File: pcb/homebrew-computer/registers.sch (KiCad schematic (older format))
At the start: 24 parts

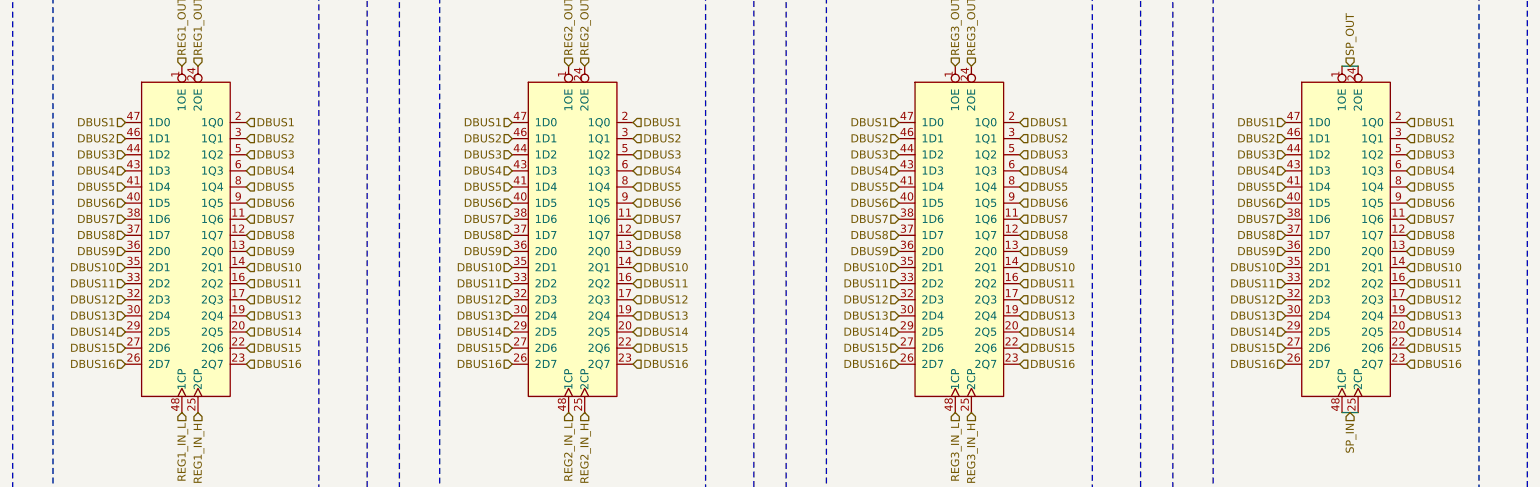
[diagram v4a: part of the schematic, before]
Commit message: Remove the address bus as it would require too big of a connector
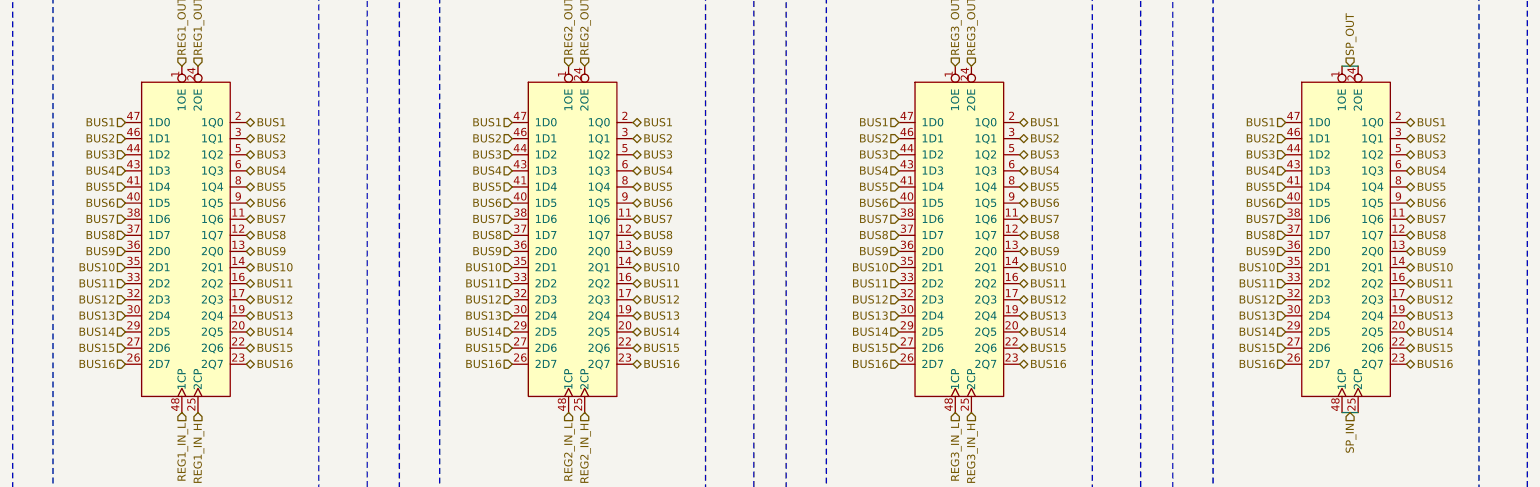
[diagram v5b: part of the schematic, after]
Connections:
- net DBUS1 renamed BUS1
- net DBUS10 renamed BUS10
- net DBUS11 renamed BUS11
- net DBUS12 renamed BUS12
- net DBUS13 renamed BUS13
- net DBUS14 renamed BUS14
- net DBUS15 renamed BUS15
- net DBUS16 renamed BUS16
- net DBUS2 renamed BUS2
- net DBUS3 renamed BUS3
- net DBUS4 renamed BUS4
- net DBUS5 renamed BUS5
- net DBUS6 renamed BUS6
- net DBUS7 renamed BUS7
- net DBUS8 renamed BUS8
- net DBUS9 renamed BUS9

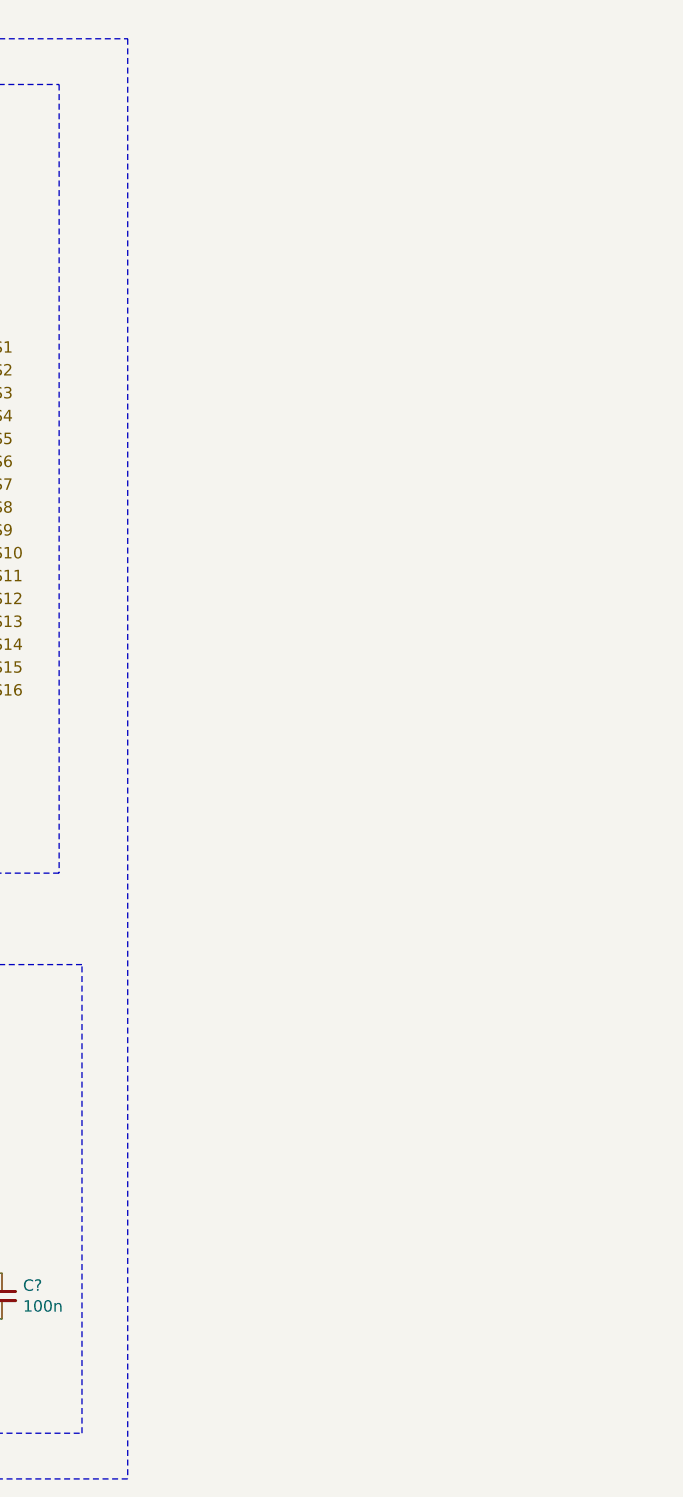
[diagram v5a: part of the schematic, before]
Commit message: Remove unnecessary address bus and unified the IO interface
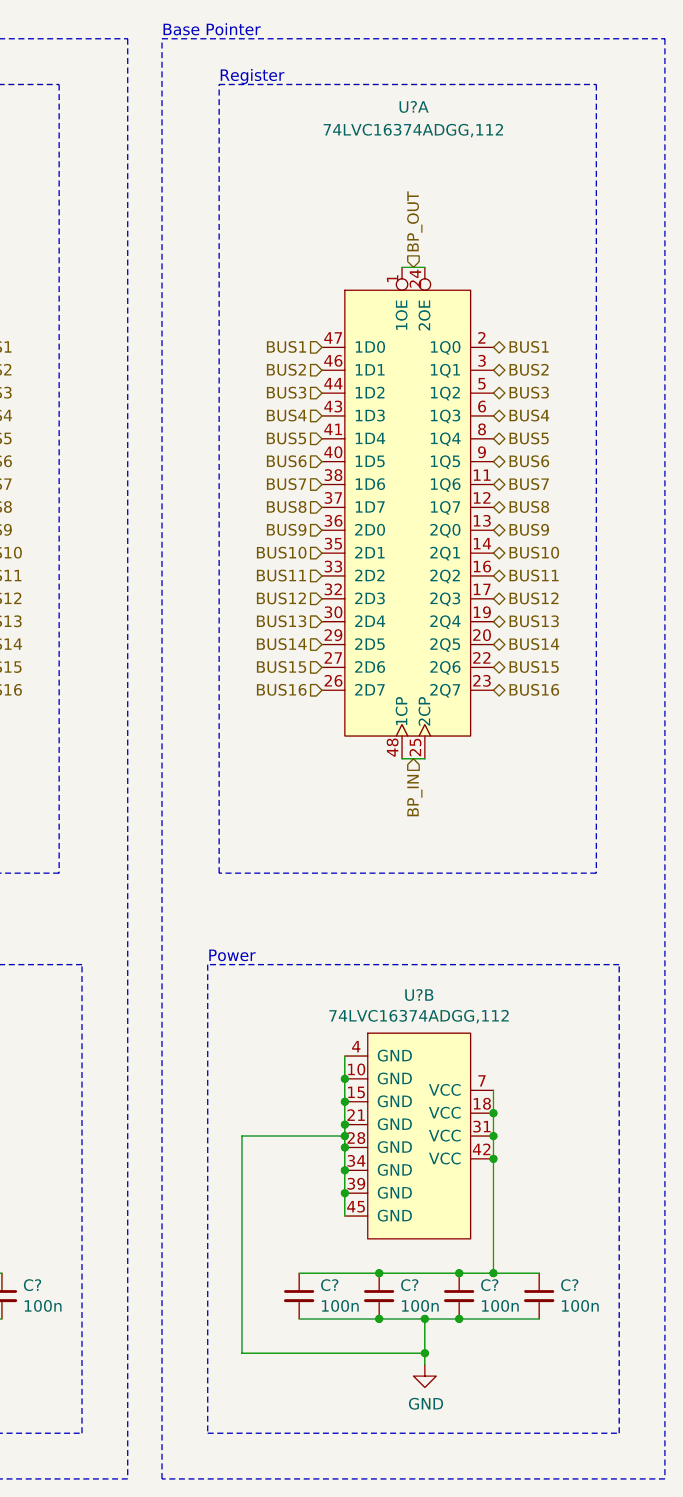
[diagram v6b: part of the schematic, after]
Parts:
- added C? (x4): 100n, symbol Device:C_Small
- added U? (x2): 74LVC16374ADGG,112, symbol 74LVC16374ADGG:74LVC16374ADGG,112
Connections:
- net BUS1: now also U?.2 (1Q0), U?.47 (1D0)
- net BUS10: now also U?.14 (2Q1), U?.35 (2D1)
- net BUS11: now also U?.16 (2Q2), U?.33 (2D2)
- net BUS12: now also U?.17 (2Q3), U?.32 (2D3)
- net BUS13: now also U?.19 (2Q4), U?.30 (2D4)
- net BUS14: now also U?.20 (2Q5), U?.29 (2D5)
- net BUS15: now also U?.22 (2Q6), U?.27 (2D6)
- net BUS16: now also U?.23 (2Q7), U?.26 (2D7)
- net BUS2: now also U?.3 (1Q1), U?.46 (1D1)
- net BUS3: now also U?.44 (1D2), U?.5 (1Q2)
- net BUS4: now also U?.43 (1D3), U?.6 (1Q3)
- net BUS5: now also U?.41 (1D4), U?.8 (1Q4)
- net BUS6: now also U?.40 (1D5), U?.9 (1Q5)
- net BUS7: now also U?.11 (1Q6), U?.38 (1D6)
- net BUS8: now also U?.12 (1Q7), U?.37 (1D7)
- net BUS9: now also U?.13 (2Q0), U?.36 (2D0)
- net GND: now also C?.2, C?.2, C?.2, C?.2, U?.10 (GND), U?.15 (GND), U?.21 (GND), U?.28 (GND), U?.34 (GND), U?.39 (GND), U?.4 (GND), U?.45 (GND)
- new net: C?.1, C?.1, C?.1, C?.1, U?.18 (VCC), U?.31 (VCC), U?.42 (VCC), U?.7 (VCC)
- new net BP_IN: U?.25 (2CP), U?.48 (1CP)
- new net BP_OUT: U?.1 (1OE), U?.24 (2OE)
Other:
- note added: "Base Pointer"

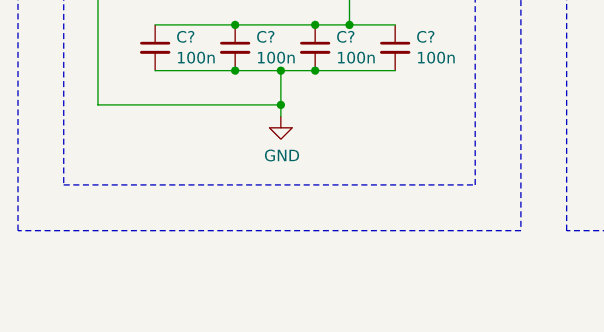
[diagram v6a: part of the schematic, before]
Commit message: Add program counter
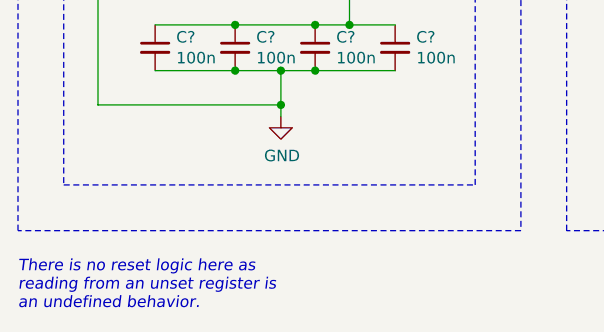
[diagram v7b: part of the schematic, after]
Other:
- note added: "There is no reset logic here as\nreading from an unset register is\nan undefined behavior."
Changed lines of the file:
@@
 Text HLabel 2200 2100 1    50   Input ~ 0
 REG1_OUT_H
-Text HLabel 2100 4250 3    50   Input ~ 0
-REG1_IN_L
-Text HLabel 2200 4250 3    50   Input ~ 0
-REG1_IN_H
 Wire Notes Line
 	1300 1300 2950 1300
-Wire Notes Line
-	2950 1300 2950 4750
-Wire Notes Line
-	2950 4750 1300 4750
-Wire Notes Line
-	1300 4750 1300 1300
 Text Notes 1300 1300 0    50   ~ 0
 Register
@@
 Text HLabel 4600 2100 1    50   Input ~ 0
 REG2_OUT_H
-Text HLabel 4500 4250 3    50   Input ~ 0
-REG2_IN_L
-Text HLabel 4600 4250 3    50   Input ~ 0
-REG2_IN_H
 Wire Notes Line
 	3700 1300 5350 1300
-Wire Notes Line
-	5350 1300 5350 4750
-Wire Notes Line
-	5350 4750 3700 4750
-Wire Notes Line
-	3700 4750 3700 1300
 Text Notes 3700 1300 0    50   ~ 0
 Register
@@
 Text HLabel 7000 2100 1    50   Input ~ 0
 REG3_OUT_H
-Text HLabel 6900 4250 3    50   Input ~ 0
-REG3_IN_L
-Text HLabel 7000 4250 3    50   Input ~ 0
-REG3_IN_H
 Wire Notes Line
 	6100 1300 7750 1300
@@
 Text HLabel 12050 3950 2    50   3State ~ 0
 BUS16
+Text HLabel 7000 4250 3    50   Input ~ 0
+REG3_IN_H
+Text HLabel 6900 4250 3    50   Input ~ 0
+REG3_IN_L
+Wire Notes Line
+	5350 1300 5350 4750
+Wire Notes Line
+	3700 4750 3700 1300
+Wire Notes Line
+	5350 4750 3700 4750
+Text HLabel 4600 4250 3    50   Input ~ 0
+REG2_IN_H
+Text HLabel 4500 4250 3    50   Input ~ 0
+REG2_IN_L
+Wire Notes Line
+	2950 1300 2950 4750
+Wire Notes Line
+	1300 4750 1300 1300
+Wire Notes Line
+	2950 4750 1300 4750
+Text HLabel 2200 4250 3    50   Input ~ 0
+REG1_IN_H
+Text HLabel 2100 4250 3    50   Input ~ 0
+REG1_IN_L
+Text Notes 1050 7750 0    50   Italic 0
+There is no reset logic here as\nreading from an unset register is\nan undefined behavior.
 $EndSCHEMATC

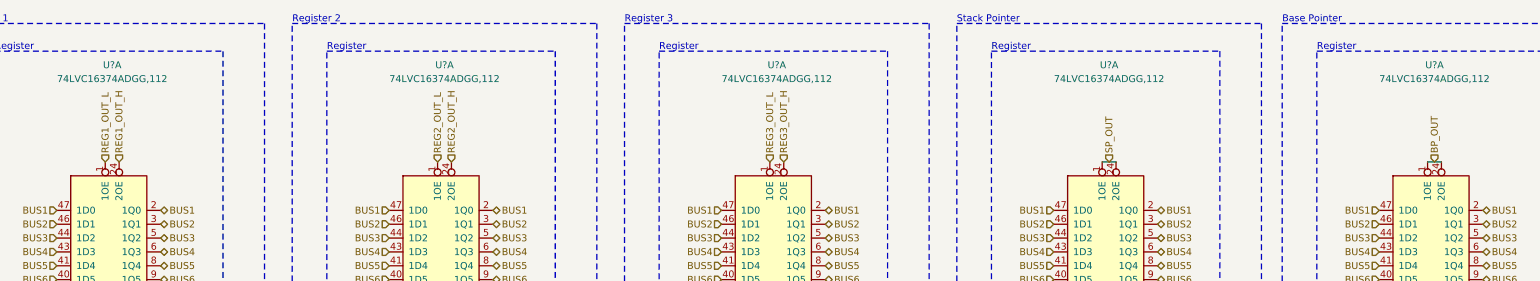
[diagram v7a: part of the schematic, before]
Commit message: Change the control logic CPLD for a bigger one
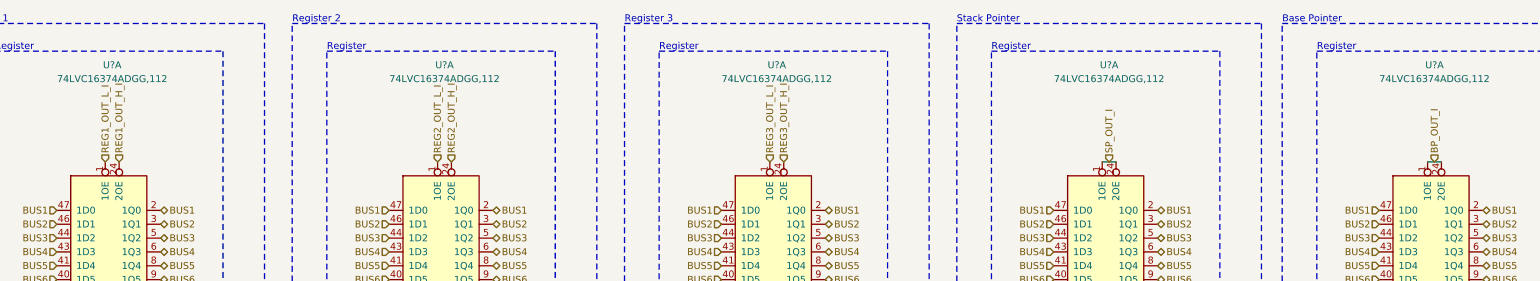
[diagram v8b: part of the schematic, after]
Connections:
- net BP_OUT renamed BP_OUT_I
- net REG1_OUT_H renamed REG1_OUT_H_I
- net REG1_OUT_L renamed REG1_OUT_L_I
- net REG2_OUT_H renamed REG2_OUT_H_I
- net REG2_OUT_L renamed REG2_OUT_L_I
- net REG3_OUT_H renamed REG3_OUT_H_I
- net REG3_OUT_L renamed REG3_OUT_L_I
- net SP_OUT renamed SP_OUT_I
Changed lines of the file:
@@
 $Descr User 13386 9843
 encoding utf-8
-Sheet 4 7
+Sheet 7 7
 Title "Registers"
 Date "2020-10-24"
@@
 Power
 Text HLabel 2100 2100 1    50   Input ~ 0
-REG1_OUT_L
+REG1_OUT_L_I
 Text HLabel 2200 2100 1    50   Input ~ 0
-REG1_OUT_H
+REG1_OUT_H_I
 Wire Notes Line
 	1300 1300 2950 1300
@@
 Power
 Text HLabel 4500 2100 1    50   Input ~ 0
-REG2_OUT_L
+REG2_OUT_L_I
 Text HLabel 4600 2100 1    50   Input ~ 0
-REG2_OUT_H
+REG2_OUT_H_I
 Wire Notes Line
 	3700 1300 5350 1300
@@
 Power
 Text HLabel 6900 2100 1    50   Input ~ 0
-REG3_OUT_L
+REG3_OUT_L_I
 Text HLabel 7000 2100 1    50   Input ~ 0
-REG3_OUT_H
+REG3_OUT_H_I
 Wire Notes Line
 	6100 1300 7750 1300
@@
 	9300 2100 9400 2100
 Text HLabel 9350 2100 1    50   Input ~ 0
-SP_OUT
+SP_OUT_I
 Wire Wire Line
 	9300 4250 9400 4250
@@
 	11650 2100 11750 2100
 Text HLabel 11700 2100 1    50   Input ~ 0
-BP_OUT
+BP_OUT_I
 Wire Wire Line
 	11650 4250 11750 4250
@@
 Wire Notes Line
 	5350 4750 3700 4750
-Text HLabel 4600 4250 3    50   Input ~ 0
-REG2_IN_H
-Text HLabel 4500 4250 3    50   Input ~ 0
-REG2_IN_L
 Wire Notes Line
 	2950 1300 2950 4750
@@
 Text Notes 1050 7750 0    50   Italic 0
 There is no reset logic here as\nreading from an unset register is\nan undefined behavior.
+Text HLabel 4600 4250 3    50   Input ~ 0
+REG2_IN_H
+Text HLabel 4500 4250 3    50   Input ~ 0
+REG2_IN_L
 $EndSCHEMATC
